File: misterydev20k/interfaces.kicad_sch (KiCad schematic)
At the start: 56 parts, among them J11 Joystick 0, J12 Joystick 1, J4 Micro_SD_Card_Det1, J5 HDMI_A, J6 Grove 1125S-4P, SW2 KEY1, SW3 KEY2, U10 74LCX07, U9 74LCX07

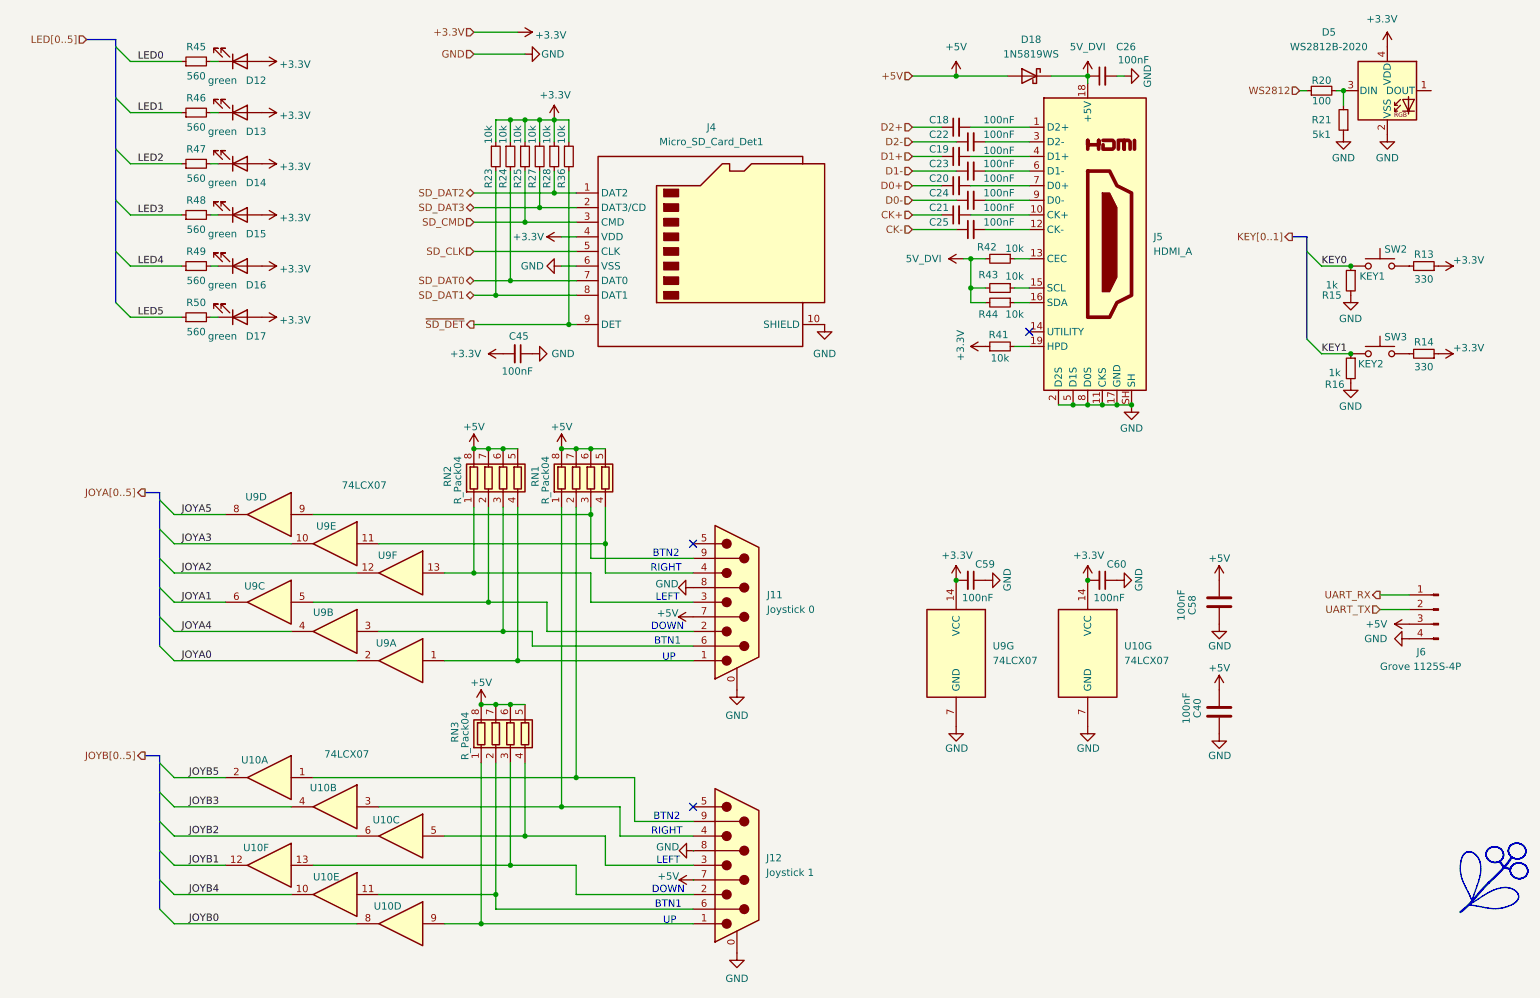
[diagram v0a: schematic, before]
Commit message: Update dev20k pinout
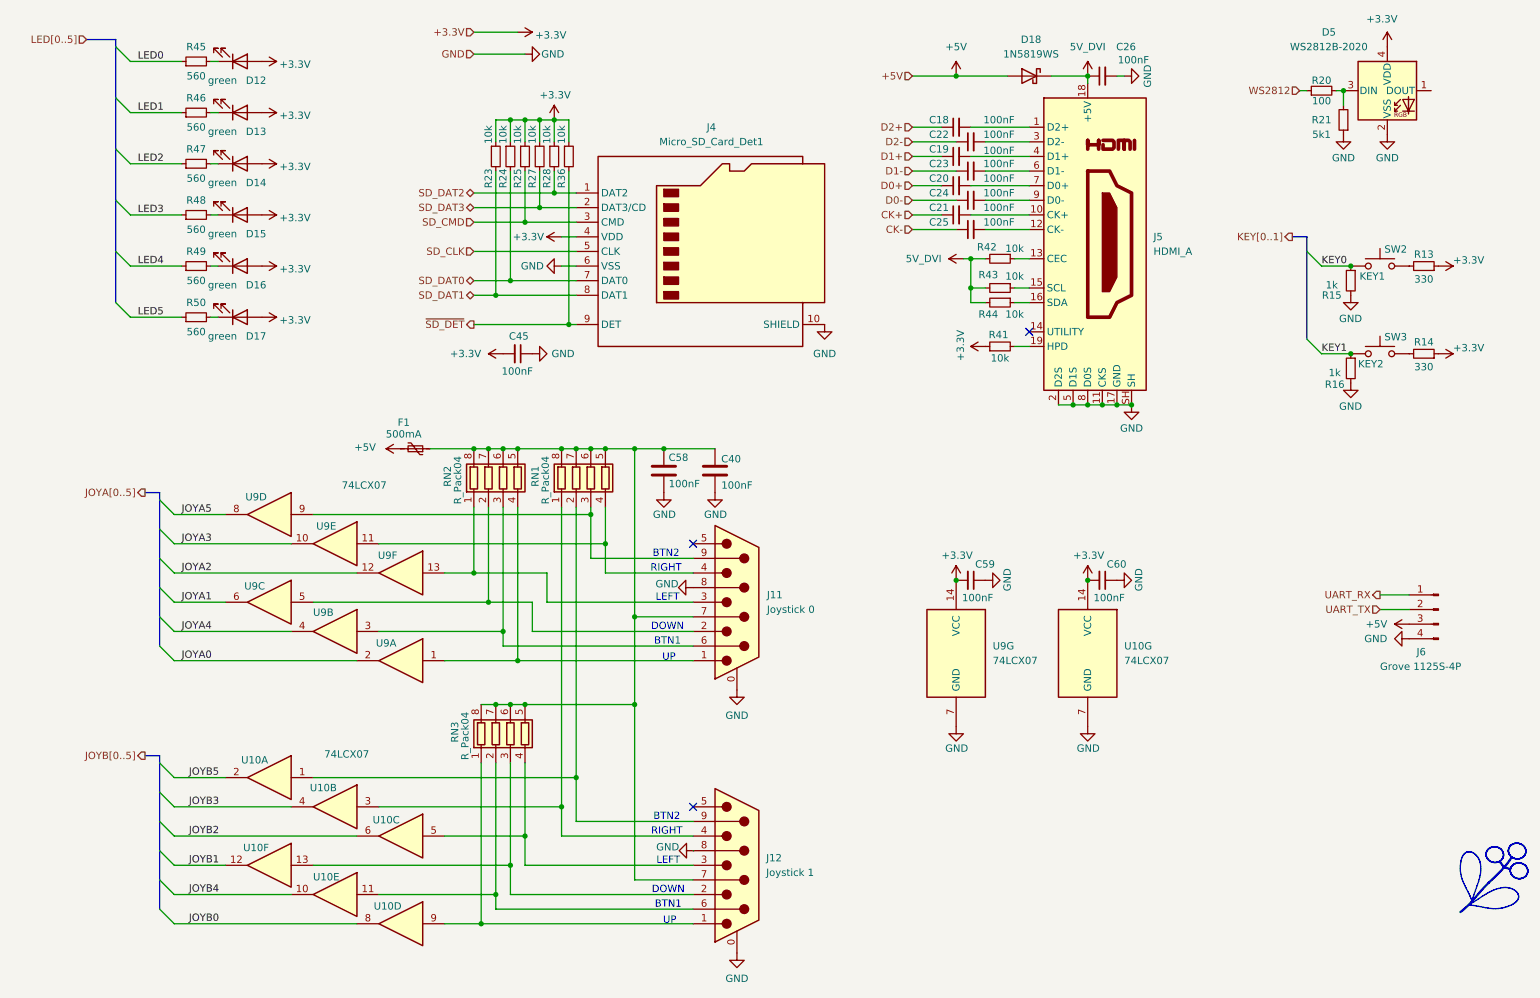
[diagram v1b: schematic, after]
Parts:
- added F1: 500mA, Fuse:Fuse_1206_3216Metric, symbol Device:Polyfuse_Small
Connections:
- net +5V: now also F1.2; no longer C40.2, C58.2, J11.7, J12.7, RN1.5 (R4.2), RN1.6 (R3.2), RN1.7 (R2.2), RN1.8 (R1.2), RN2.5 (R4.2), RN2.6 (R3.2), RN2.7 (R2.2), RN2.8 (R1.2), RN3.5 (R4.2), RN3.6 (R3.2), RN3.7 (R2.2), RN3.8 (R1.2)
- new net: C40.2, C58.2, F1.1, J11.7, J12.7, RN1.5 (R4.2), RN1.6 (R3.2), RN1.7 (R2.2), RN1.8 (R1.2), RN2.5 (R4.2), RN2.6 (R3.2), RN2.7 (R2.2), RN2.8 (R1.2), RN3.5 (R4.2), RN3.6 (R3.2), RN3.7 (R2.2), RN3.8 (R1.2)
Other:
- moved on the sheet: C40, C58

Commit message: Dev20k LCSC part mapping
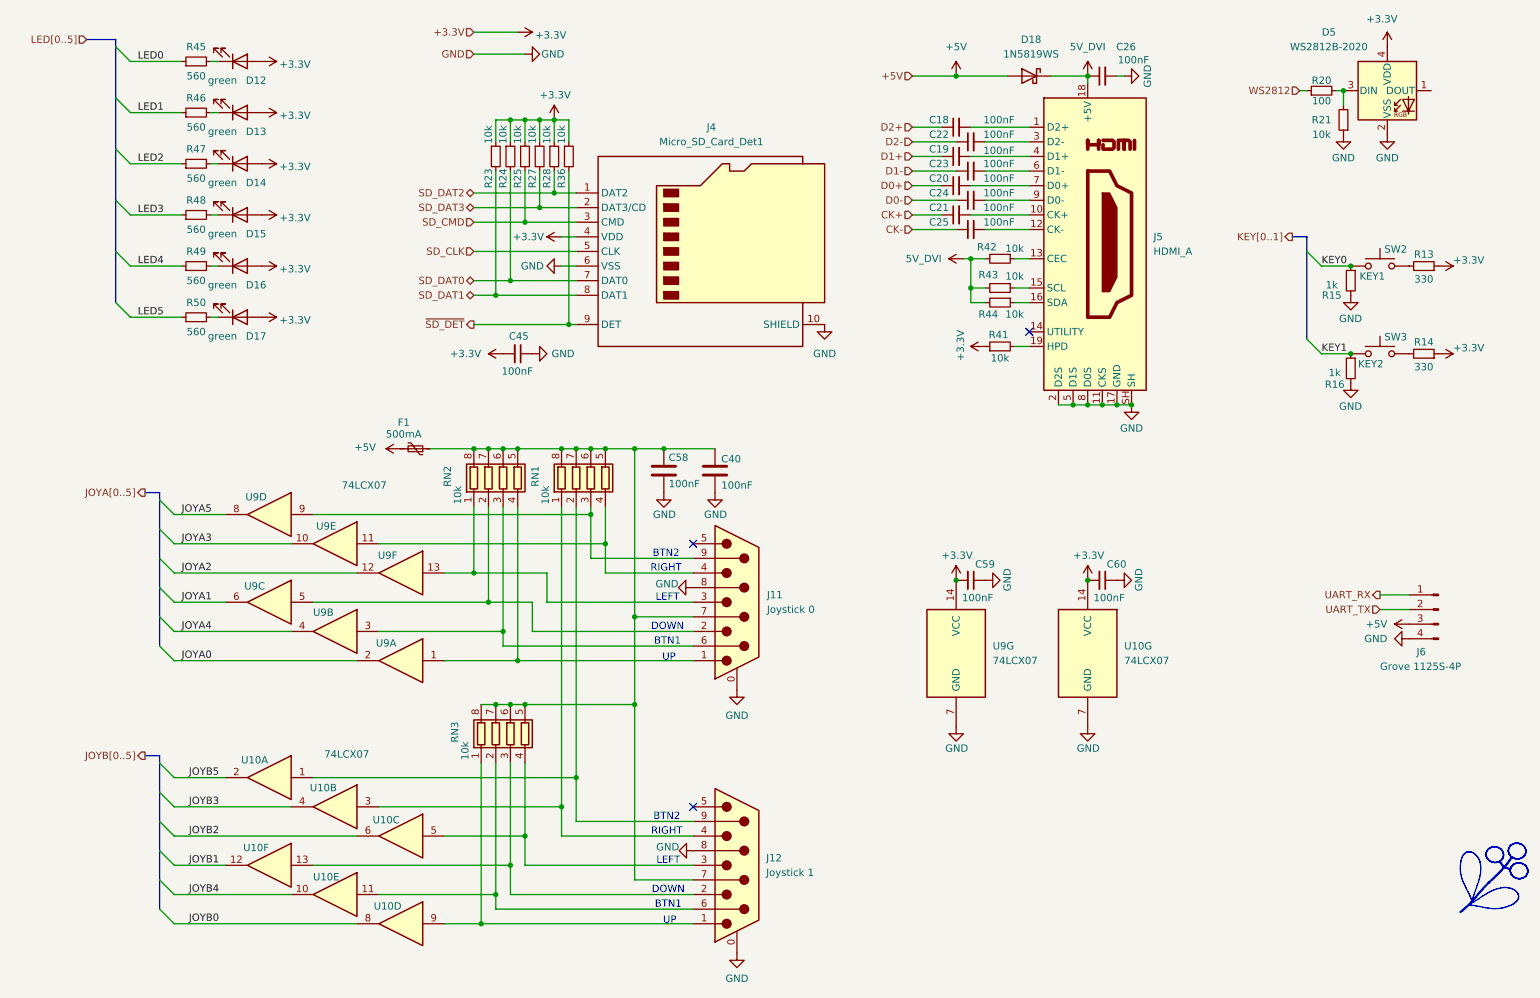
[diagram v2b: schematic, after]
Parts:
- C18, C19, C20, C21, C22, C23, C24, C25, C26, C45, C59, C60: LCSC C1525 -> (none); LCSC Part # (none) -> C1525; checked (none) -> once
- C40, C58: LCSC Part # C4967 -> C1525; checked (none) -> once
- D12, D13, D14, D15, D16, D17: LCSC C2297 -> (none); LCSC Part # (none) -> C2297; checked (none) -> once
- D18: LCSC Part # (none) -> C2927280; checked (none) -> once
- D5: LCSC Part # (none) -> C965555; checked (none) -> once
- F1: LCSC C70076 -> (none); LCSC Part # (none) -> C70076; checked (none) -> once
- J11, J12, J4: checked (none) -> once
- J5: LCSC Part # (none) -> C720616; checked (none) -> once
- R13, R14: LCSC Part # (none) -> C105875; checked (none) -> once
- R15, R16: LCSC C11702 -> (none); LCSC Part # (none) -> C11702; checked (none) -> once
- R20: LCSC C11702 -> (none); LCSC Part # (none) -> C25076; checked (none) -> once
- R21: value 5k1 -> 10k; LCSC C11702 -> (none); LCSC Part # (none) -> C25744; checked (none) -> once
- R23, R24, R25, R27, R28, R36: LCSC C11702 -> (none); LCSC Part # (none) -> C25744; checked (none) -> once
- R41, R42, R43, R44: LCSC Part # (none) -> C25744; checked (none) -> once
- R45, R46, R47, R48, R49, R50: LCSC C163460 -> (none); LCSC Part # (none) -> C163460; checked (none) -> once
- RN1, RN2, RN3: value R_Pack04 -> 10k; LCSC Part # (none) -> C110924; checked (none) -> once
- SW2, SW3: LCSC C318884 -> (none); LCSC Part # (none) -> C318884; checked (none) -> once
- U10, U9: LCSC Part # (none) -> C2676034; checked (none) -> once

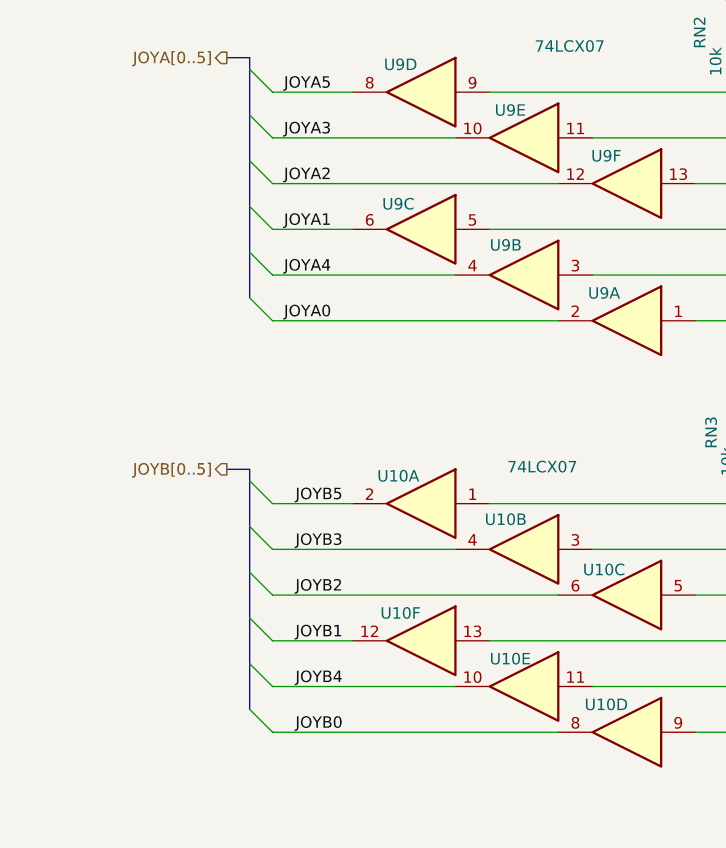
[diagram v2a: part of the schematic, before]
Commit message: Fix joystick connections
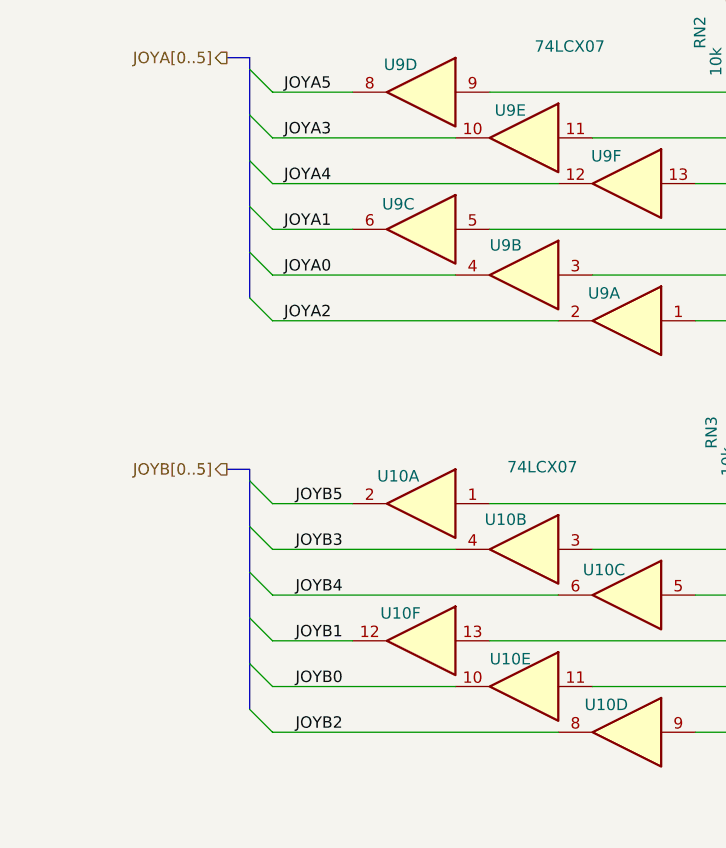
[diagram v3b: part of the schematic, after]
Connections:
- net JOYA0: now also U9.4; no longer U9.2
- net JOYA2: now also U9.2; no longer U9.12
- net JOYA4: now also U9.12; no longer U9.4
- net JOYB0: now also U10.10; no longer U10.8
- net JOYB2: now also U10.8; no longer U10.6
- net JOYB4: now also U10.6; no longer U10.10
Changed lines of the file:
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@@
 		)
 	)
-	(label "JOYB2"
+	(label "JOYB4"
 		(at 50.8 166.37 0)
 		(effects
@@
 		)
 	)
-	(label "JOYB0"
+	(label "JOYB2"
 		(at 50.8 181.61 0)
 		(effects
@@
 		)
 	)
-	(label "JOYA2"
+	(label "JOYA4"
 		(at 49.53 120.65 0)
 		(effects
@@
 		)
 	)
-	(label "JOYB4"
+	(label "JOYB0"
 		(at 50.8 176.53 0)
 		(effects
@@
 		)
 	)
-	(label "JOYA4"
+	(label "JOYA0"
 		(at 49.53 130.81 0)
 		(effects
@@
 		)
 	)
-	(label "JOYA0"
+	(label "JOYA2"
 		(at 49.53 135.89 0)
 		(effects
